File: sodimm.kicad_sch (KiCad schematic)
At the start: 2 parts, among them J9 2309409-1

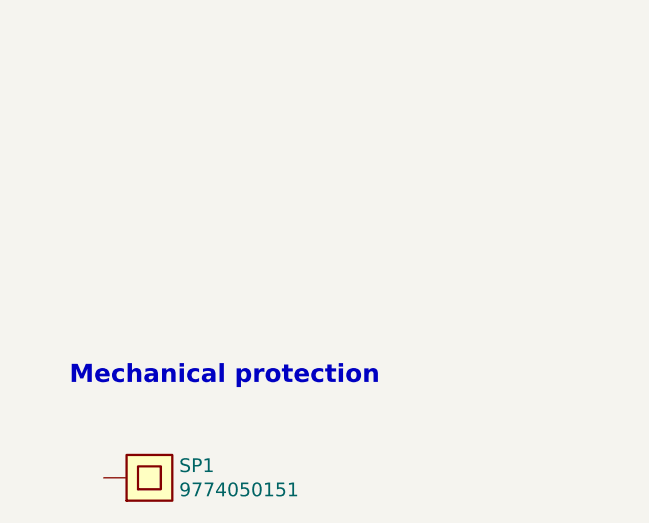
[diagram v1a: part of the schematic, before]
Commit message: Added separate symbol with DDR5 testbed footprint and 3D model
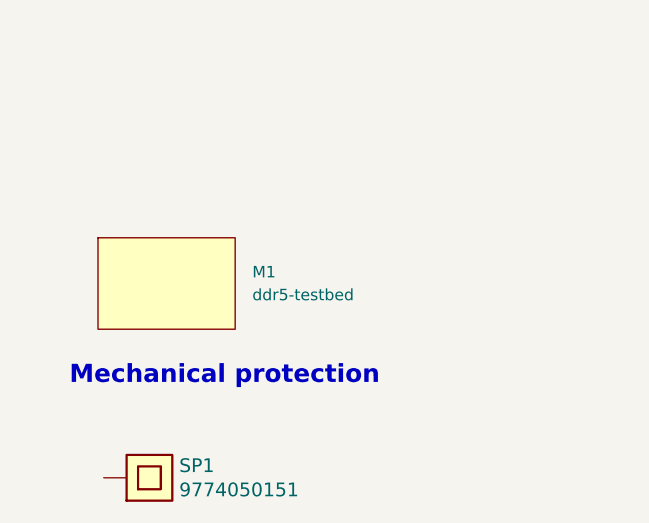
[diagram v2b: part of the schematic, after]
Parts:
- added M1: ddr5-testbed, lpddr4-test-board-footprints:DDR5-testbed, symbol lpddr4-test-board:ddr5-testbed
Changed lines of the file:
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@@
     (pin "1")
   )
+  (symbol (lib_id "lpddr4-test-board:ddr5-testbed") (at 34.925 219.075 0) (unit 1)
+    (in_bom no) (on_board yes) (fields_autoplaced)
+    (property "Reference" "M1" (id 0) (at 44.45 217.8049 0)
+      (effects (font (size 1.27 1.27)) (justify left))
+    )
+    (property "Value" "ddr5-testbed" (id 1) (at 44.45 220.3449 0)
+      (effects (font (size 1.27 1.27)) (justify left))
+    )
+    (property "Footprint" "lpddr4-test-board-footprints:DDR5-testbed" (id 2) (at 34.925 225.425 0)
+      (effects (font (size 1.27 1.27)) hide)
+    )
+    (property "Datasheet" "" (id 3) (at 34.925 216.535 0)
+      (effects (font (size 1.27 1.27)) hide)
+    )
+  )
 )

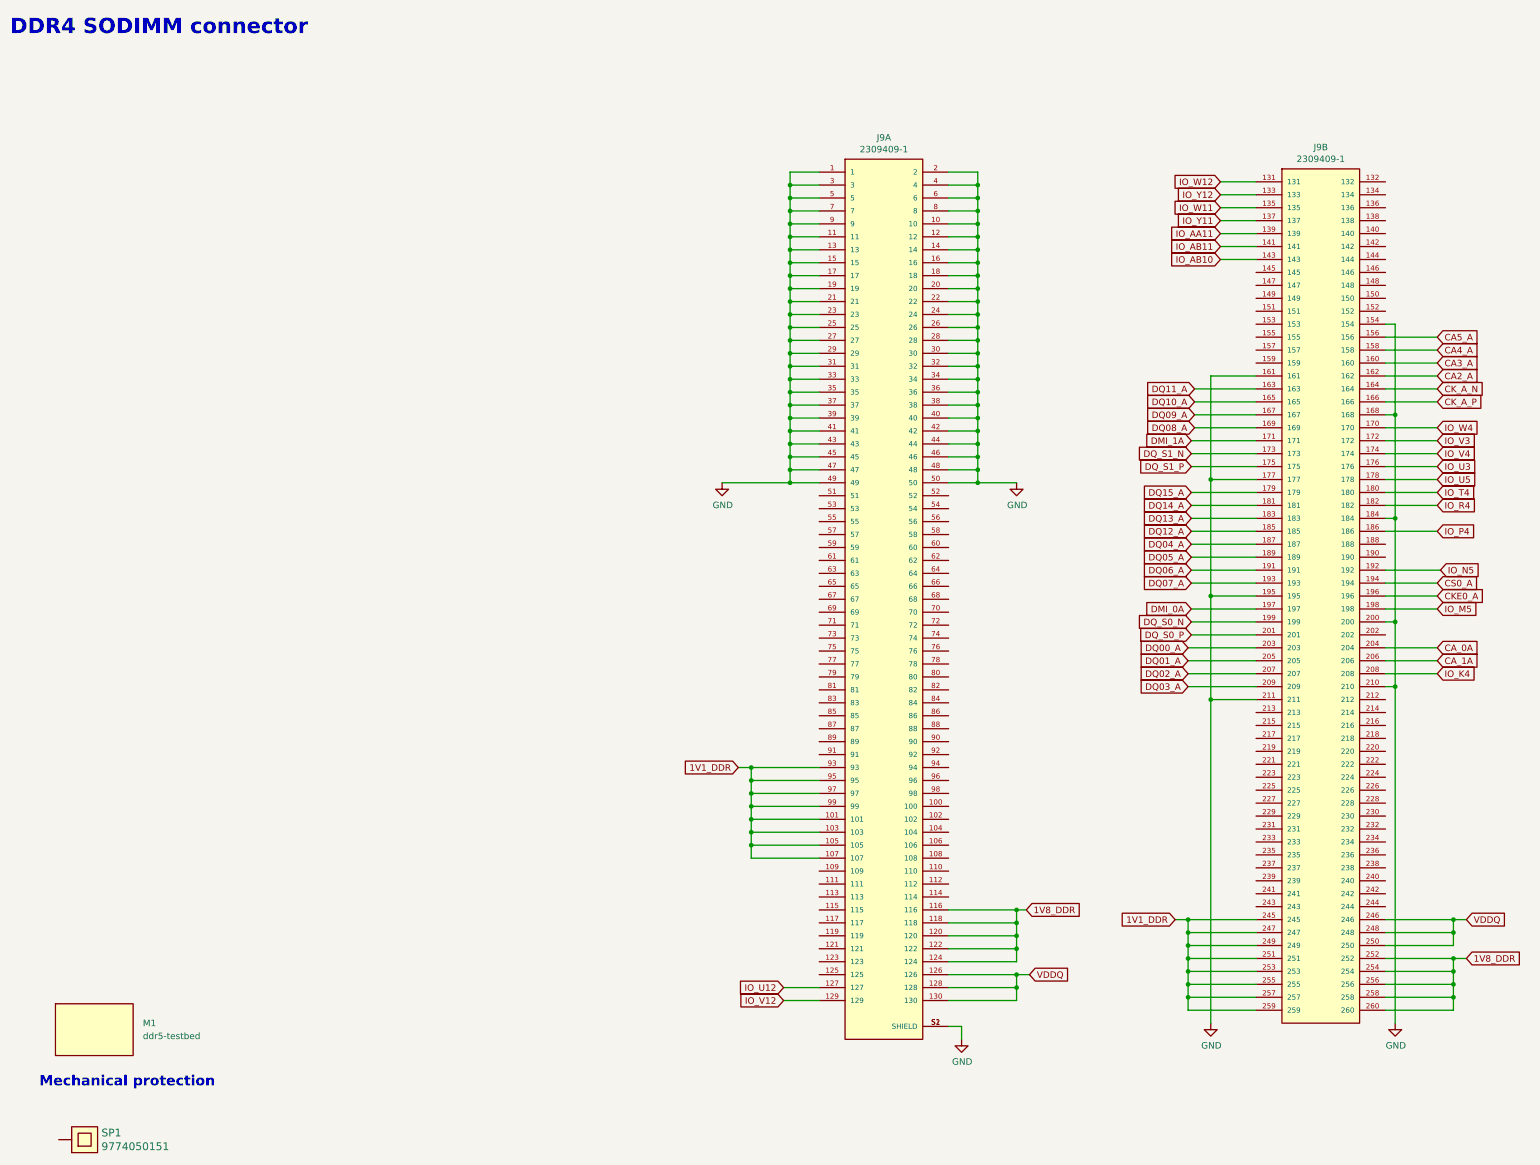
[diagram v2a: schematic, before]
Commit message: Introduce standardized components
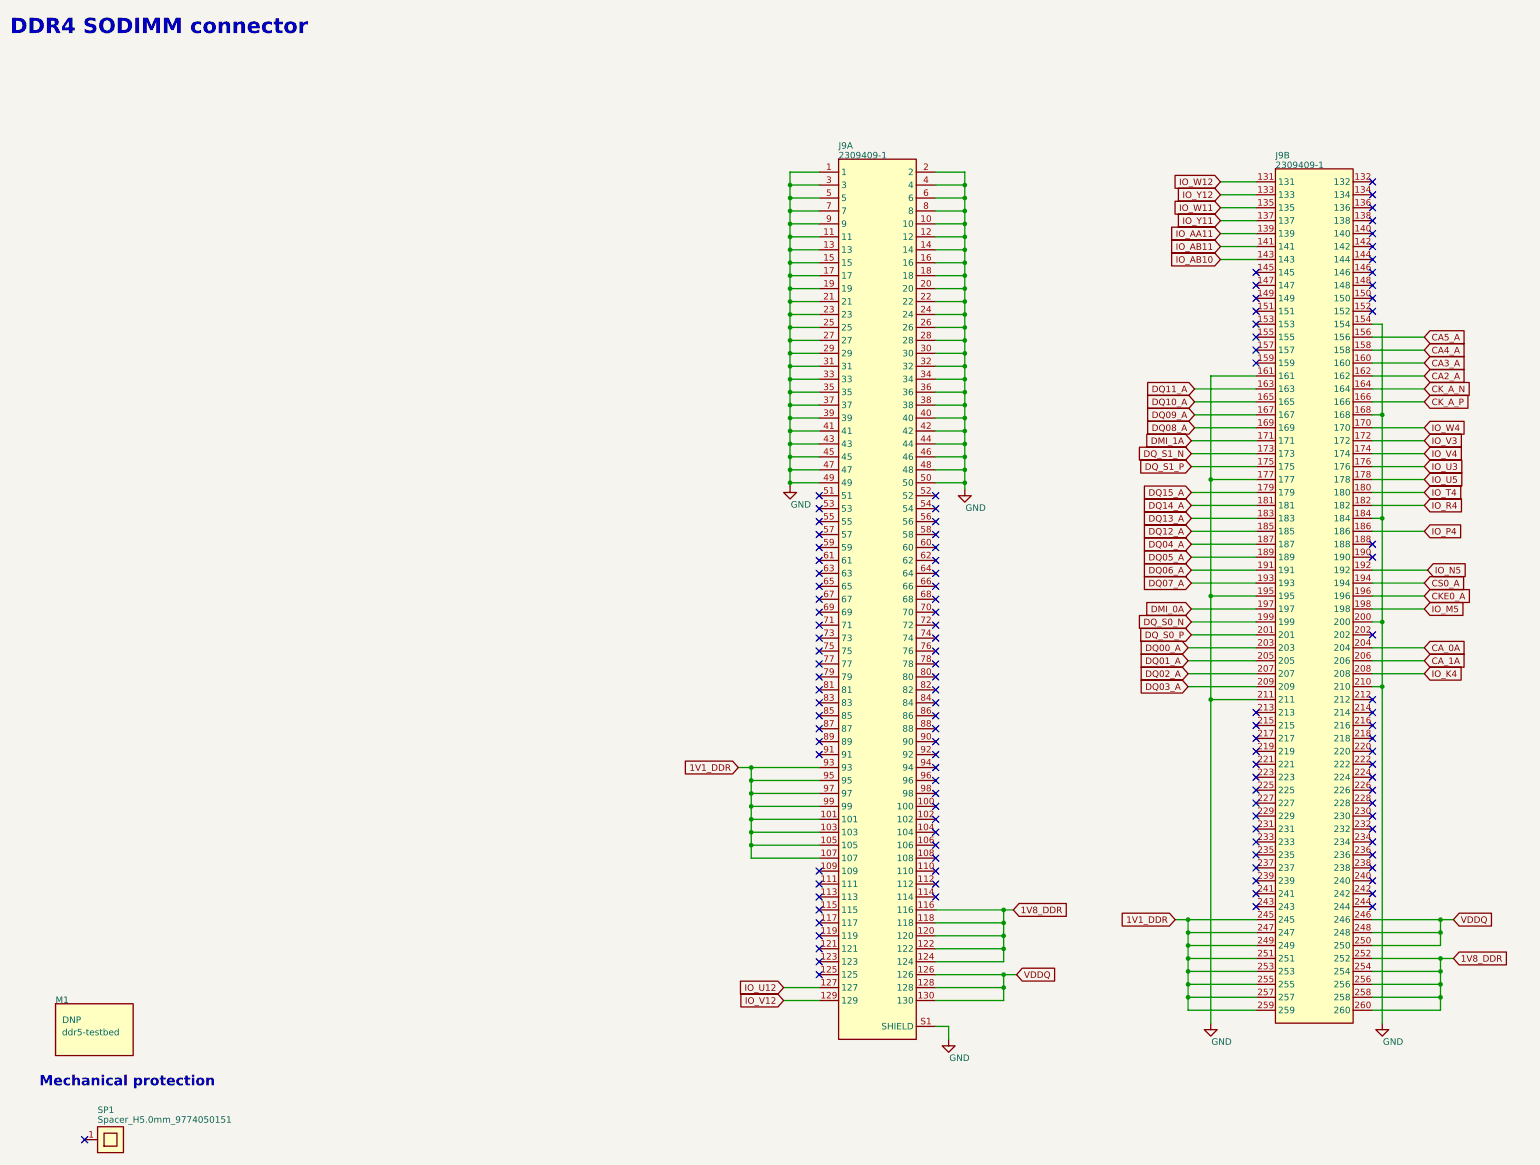
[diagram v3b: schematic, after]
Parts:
- J9: value 2309409-1 -> Bus_DDR4_SODIMM_TE_2309409; footprint lpddr4-test-board-footprints:TE_2309409-1 -> lpddr4-test-board-footprints:Bus_DDR4_SODIMM_TE_2309409; symbol lpddr4-test-board:2309409-1 -> lpddr4-test-board:Bus_DDR4_SODIMM_TE_2309409; Author (none) -> Antmicro; License (none) -> Apache-2.0
- M1: Author (none) -> Antmicro; DNP (none) -> DNP; License (none) -> Apache-2.0; Manufacturer (none) -> Antmicro
- SP1: value 9774050151 -> Spacer_H5.0mm_9774050151; footprint lpddr4-test-board-footprints:9774050151 -> lpddr4-test-board-footprints:Spacer_SMD_M2.5_H5mm_Wurth_9774050151; symbol lpddr4-test-board:9774050151 -> lpddr4-test-board:Spacer_H5.0mm_9774050151; Author (none) -> Antmicro; License (none) -> Apache-2.0; Manufacturer Wurth Elektronik -> Würth Elektronik
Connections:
- no-connect marks 0 -> 118
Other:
- moved on the sheet: J9B

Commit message: [#55158] components update
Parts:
- M1: now not fitted
- SP1: footprint lpddr4-test-board-footprints:Spacer_SMD_M2.5_H5mm_Wurth_9774050151 -> lpddr4-test-board-footprints:Spacer_Drill3.7mm_H5mm_9774050151R; symbol lpddr4-test-board:Spacer_H5.0mm_9774050151 -> lpddr4-test-board:Spacer_Drill3.7mm_H5mm_9774050151R; MPN 9774050151 -> 9774050151R
